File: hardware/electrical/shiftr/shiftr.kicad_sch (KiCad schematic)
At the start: 12 parts, among them J1 2171750001, J2 PJ-002AH, J3 SJ1-3523N

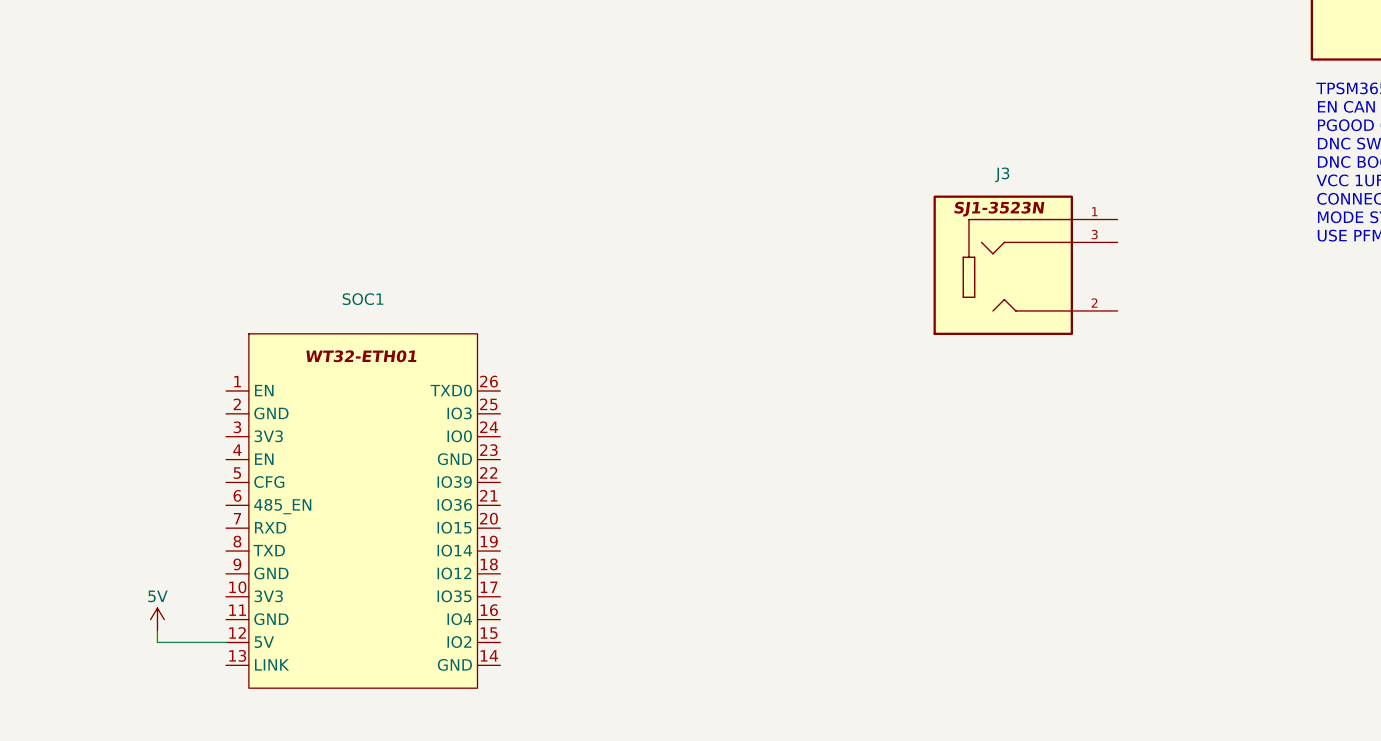
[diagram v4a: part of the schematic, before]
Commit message: add shift button nets, pull down resistors
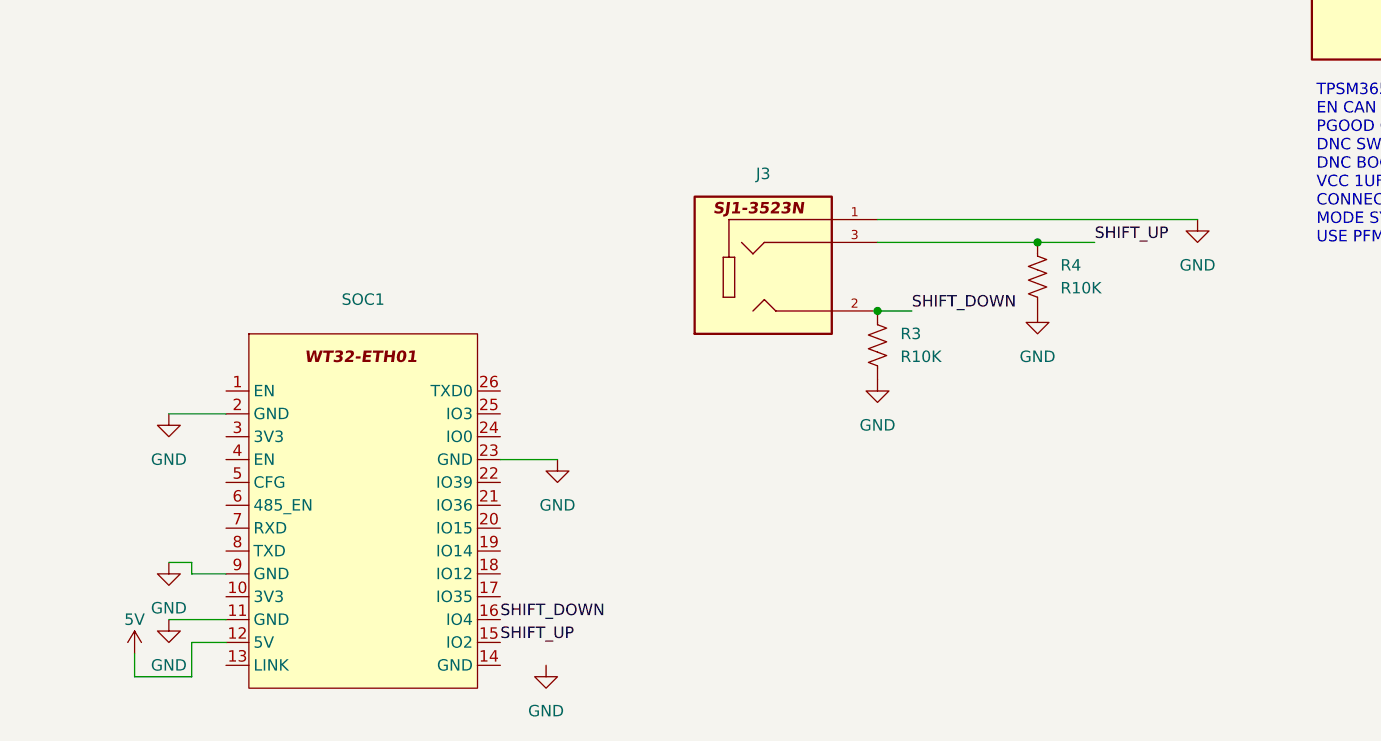
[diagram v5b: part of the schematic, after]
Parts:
- added R3, R4: R10K, Resistor_SMD:R_1206_3216Metric, symbol symbol_library:R10K
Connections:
- net GND: now also J3.1, SOC1.11 (GND), SOC1.2 (GND), SOC1.23 (GND), SOC1.9 (GND), R3.2, R4.2
- net SHIFT_DOWN: now reaches J3.2
- net SHIFT_DOWN: now also SOC1.16 (IO4), R3.1
- net SHIFT_UP: now reaches J3.3
- net SHIFT_UP: now also SOC1.15 (IO2), R4.1
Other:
- moved on the sheet: J3

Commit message: route traces
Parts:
- added C6: 10uF, Capacitor_SMD:C_1210_3225Metric, symbol symbol_library:C10uF
- added C7: 1uF, Capacitor_SMD:C_0603_1608Metric, symbol symbol_library:C1uF
- added H1, H2, H3, H4: ~, footprint_library:Hole-3mm, symbol symbol_library:hole_3mm
- added R5, R7: R10K, Resistor_SMD:R_1206_3216Metric, symbol symbol_library:R10K
- added S1: SDA01H1SBD, footprint_library:SW_SDA01H1SBD, symbol symbol_library:SDA01H1SBD
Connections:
- net 5V_USB is gone; now on net 5V: J1.A9 (VBUS1), J1.B9 (VBUS2)
- net 48V: now also PS1.2 (EN), PS1.3 (VIN)
- net 5V: now also C6.1, C7.1, R7.1
- net GND: now also C1.2, C2.2, C6.2, C7.2, R5.2, S1.COM1
- net at SOC1.18 (IO12): now also R5.1
- net at SOC1.24 (IO0): now also R7.2, S1.NO1
- no-connect marks 4 -> 21
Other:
- moved on the sheet: C1, C2, J3, R1, R3, R4

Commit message: add programming pinheader
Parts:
- added J4: Conn_01x05_Pin, Connector_PinHeader_2.54mm:PinHeader_1x05_P2.54mm_Vertical, symbol Connector:Conn_01x05_Pin
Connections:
- net GND: now also SOC1.14 (GND), J4.1 (Pin_1)
- net EN: now reaches SOC1.1 (EN)
- net EN: now also J4.5 (Pin_5)
- net 3V3: now reaches SOC1.10 (3V3)
- net 3V3: now also J4.2 (Pin_2)
- net RXD: now reaches SOC1.7 (RXD)
- net RXD: now also J4.4 (Pin_4)
- net TXD: now reaches SOC1.8 (TXD)
- net TXD: now also J4.3 (Pin_3)
- no-connect marks 21 -> 16
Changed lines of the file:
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@@
-	)
-	(no_connect
-		(at 53.34 133.35)
 	)
 	(no_connect
@@
 	)
 	(no_connect
-		(at 53.34 115.57)
-	)
-	(no_connect
 		(at 209.55 71.12)
 	)
@@
 	)
 	(no_connect
-		(at 53.34 138.43)
-	)
-	(no_connect
 		(at 53.34 120.65)
 	)
@@
 		(at 83.82 130.81)
 	)
-	(no_connect
-		(at 53.34 130.81)
-	)
-	(no_connect
-		(at 83.82 146.05)
-	)
 	(wire
 		(pts
@@
 	(wire
 		(pts
+			(xy 49.53 130.81) (xy 53.34 130.81)
+		)
+		(stroke
+			(width 0)
+			(type default)
+		)
+	)
+	(wire
+		(pts
 			(xy 209.55 55.88) (xy 214.63 55.88)
 		)
@@
 	(wire
 		(pts
+			(xy 49.53 115.57) (xy 53.34 115.57)
+		)
+		(stroke
+			(width 0)
+			(type default)
+		)
+	)
+	(wire
+		(pts
 			(xy 83.82 41.91) (xy 88.9 41.91)
 		)
@@
 	(wire
 		(pts
+			(xy 49.53 133.35) (xy 53.34 133.35)
+		)
+		(stroke
+			(width 0)
+			(type default)
+		)
+	)
+	(wire
+		(pts
+			(xy 49.53 138.43) (xy 53.34 138.43)
+		)
+		(stroke
+			(width 0)
+			(type default)
+		)
+	)
+	(wire
+		(pts
 			(xy 29.21 49.53) (xy 33.02 49.53)
 		)
@@
 			(width 0)
 			(type default)
+		)
+	)
+	(label "3V3"
+		(at 49.53 138.43 0)
+		(effects
+			(font
+				(size 1.27 1.27)
+			)
+			(justify left bottom)
+		)
+	)
+	(label "GND"
+		(at 91.44 92.71 0)
+		(effects
+			(font
+				(size 1.27 1.27)
+			)
+			(justify left bottom)
 		)
 	)
@@
 		)
 	)
+	(label "EN"
+		(at 49.53 115.57 0)
+		(effects
+			(font
+				(size 1.27 1.27)
+			)
+			(justify left bottom)
+		)
+	)
+	(label "RXD"
+		(at 49.53 130.81 0)
+		(effects
+			(font
+				(size 1.27 1.27)
+			)
+			(justify left bottom)
+		)
+	)
+	(label "TXD"
+		(at 49.53 133.35 0)
+		(effects
+			(font
+				(size 1.27 1.27)
+			)
+			(justify left bottom)
+		)
+	)
+	(label "3V3"
+		(at 91.44 95.25 0)
+		(effects
+			(font
+				(size 1.27 1.27)
+			)
+			(justify left bottom)
+		)
+	)
+	(label "RXD"
+		(at 91.44 100.33 0)
+		(effects
+			(font
+				(size 1.27 1.27)
+			)
+			(justify left bottom)
+		)
+	)
 	(label "BIAS"
 		(at 214.63 58.42 270)
@@
 		)
 	)
+	(label "TXD"
+		(at 91.44 97.79 0)
+		(effects
+			(font
+				(size 1.27 1.27)
+			)
+			(justify left bottom)
+		)
+	)
 	(label "SHIFT_DOWN"
 		(at 228.6 138.43 0)
@@
 		)
 	)
+	(label "EN"
+		(at 91.44 102.87 0)
+		(effects
+			(font
+				(size 1.27 1.27)
+			)
+			(justify left bottom)
+		)
+	)
 	(label "SHIFT_UP"
 		(at 248.92 130.81 0)
@@
 			)
 			(justify left bottom)
+		)
+	)
+	(symbol
+		(lib_id "Connector:Conn_01x05_Pin")
+		(at 86.36 97.79 0)
+		(unit 1)
+		(exclude_from_sim no)
+		(in_bom yes)
+		(on_board yes)
+		(dnp no)
+		(fields_autoplaced yes)
+		(property "Reference" "J4"
+			(at 86.995 87.63 0)
+			(effects
+				(font
+					(size 1.27 1.27)
+				)
+			)
+		)
+		(property "Value" "Conn_01x05_Pin"
+			(at 86.995 90.17 0)
+			(effects
+				(font
+					(size 1.27 1.27)
+				)
+			)
+		)
+		(property "Footprint" "Connector_PinHeader_2.54mm:PinHeader_1x05_P2.54mm_Vertical"
+			(at 86.36 97.79 0)
+			(effects
+				(font
+					(size 1.27 1.27)
+				)
+				(hide yes)
+			)
+		)
+		(property "Datasheet" "~"
+			(at 86.36 97.79 0)
+			(effects
+				(font
+					(size 1.27 1.27)
+				)
+				(hide yes)
+			)
+		)
+		(property "Description" "Generic connector, single row, 01x05, script generated"
+			(at 86.36 97.79 0)
+			(effects
+				(font
+					(size 1.27 1.27)
+				)
+				(hide yes)
+			)
+		)
+		(pin "4"
+		)
+		(pin "1"
+		)
+		(pin "5"
+		)
+		(pin "2"
+		)
+		(pin "3"
+		)
+		(instances
+			(project ""
+				(path "/3bfa63c6-9d72-4aec-ae9c-b2577824d50b"
+					(reference "J4")
+					(unit 1)
+				)
+			)
 		)
 	)
@@
 	(symbol
 		(lib_id "power:GND")
-		(at 88.9 146.05 0)
+		(at 83.82 146.05 0)
 		(unit 1)
 		(exclude_from_sim no)
@@
 		(fields_autoplaced yes)
 		(property "Reference" "#PWR020"
-			(at 88.9 152.4 0)
+			(at 83.82 152.4 0)
 			(effects
 				(font
@@
 		)
 		(property "Value" "GND"
-			(at 88.9 151.13 0)
+			(at 83.82 151.13 0)
 			(effects
 				(font
@@
 		)
 		(property "Footprint" ""
-			(at 88.9 146.05 0)
+			(at 83.82 146.05 0)
 			(effects
 				(font
@@
 		)
 		(property "Datasheet" ""
-			(at 88.9 146.05 0)
+			(at 83.82 146.05 0)
 			(effects
 				(font
@@
 		)
 		(property "Description" "Power symbol creates a global label with name \"GND\" , ground"
-			(at 88.9 146.05 0)
-			(effects
-				(font
+			(at 83.82 146.05 0)
+			(effects
+				(font

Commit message: update some traces
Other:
- moved on the sheet: J4
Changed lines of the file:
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@@
 	)
 	(label "GND"
-		(at 91.44 92.71 0)
+		(at 113.03 81.28 0)
 		(effects
 			(font
@@
 	)
 	(label "3V3"
-		(at 91.44 95.25 0)
+		(at 113.03 83.82 0)
 		(effects
 			(font
@@
 	)
 	(label "RXD"
-		(at 91.44 100.33 0)
+		(at 113.03 88.9 0)
 		(effects
 			(font
@@
 	)
 	(label "TXD"
-		(at 91.44 97.79 0)
+		(at 113.03 86.36 0)
 		(effects
 			(font
@@
 	)
 	(label "EN"
-		(at 91.44 102.87 0)
+		(at 113.03 91.44 0)
 		(effects
 			(font
@@
 	(symbol
 		(lib_id "Connector:Conn_01x05_Pin")
-		(at 86.36 97.79 0)
+		(at 107.95 86.36 0)
 		(unit 1)
 		(exclude_from_sim no)
@@
 		(fields_autoplaced yes)
 		(property "Reference" "J4"
-			(at 86.995 87.63 0)
+			(at 108.585 76.2 0)
 			(effects
 				(font
@@
 		)
 		(property "Value" "Conn_01x05_Pin"
-			(at 86.995 90.17 0)
+			(at 108.585 78.74 0)
 			(effects
 				(font
@@
 		)
 		(property "Footprint" "Connector_PinHeader_2.54mm:PinHeader_1x05_P2.54mm_Vertical"
-			(at 86.36 97.79 0)
+			(at 107.95 86.36 0)
 			(effects
 				(font
@@
 		)
 		(property "Datasheet" "~"
-			(at 86.36 97.79 0)
+			(at 107.95 86.36 0)
 			(effects
 				(font
@@
 		)
 		(property "Description" "Generic connector, single row, 01x05, script generated"
-			(at 86.36 97.79 0)
+			(at 107.95 86.36 0)
 			(effects
 				(font
